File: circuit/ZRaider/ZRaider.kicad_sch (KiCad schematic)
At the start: 20 parts, among them J1 DE9_Socket, SW1 UP, SW2 DOWN, SW3 LEFT, SW4 RIGHT, SW5 Trigger, SW6 Calibrate

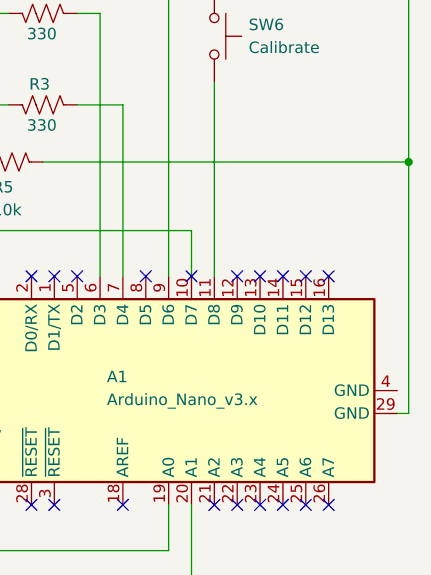
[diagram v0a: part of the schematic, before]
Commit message: adding last remaining connections
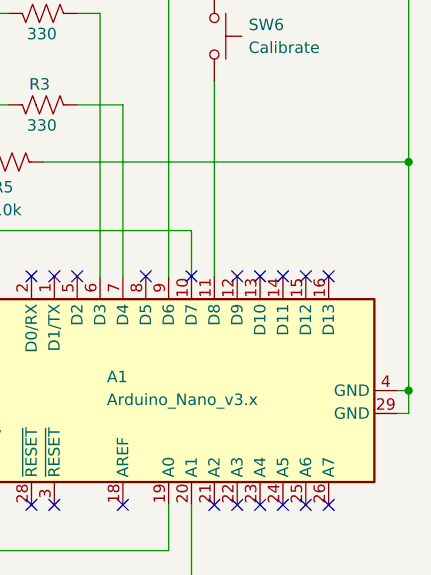
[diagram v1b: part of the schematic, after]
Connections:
- net at A1.29 (GND), C1.2, C2.2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: now also A1.4 (GND)
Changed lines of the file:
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@@
+	)
+	(junction
+		(at 236.22 119.38)
+		(diameter 0)
+		(color 0 0 0 0)
 	)
 	(junction
@@
 	(wire
 		(pts
+			(xy 236.22 119.38) (xy 236.22 121.92)
+		)
+		(stroke
+			(width 0)
+			(type default)
+		)
+	)
+	(wire
+		(pts
 			(xy 69.85 49.53) (xy 87.63 49.53)
 		)
@@
 	(wire
 		(pts
+			(xy 234.95 119.38) (xy 236.22 119.38)
+		)
+		(stroke
+			(width 0)
+			(type default)
+		)
+	)
+	(wire
+		(pts
 			(xy 212.09 146.05) (xy 212.09 132.08)
 		)
@@
 	(wire
 		(pts
-			(xy 236.22 93.98) (xy 236.22 121.92)
-		)
-		(stroke
+			(xy 236.22 93.98) (xy 236.22 119.38)
+		)
+		(stroke

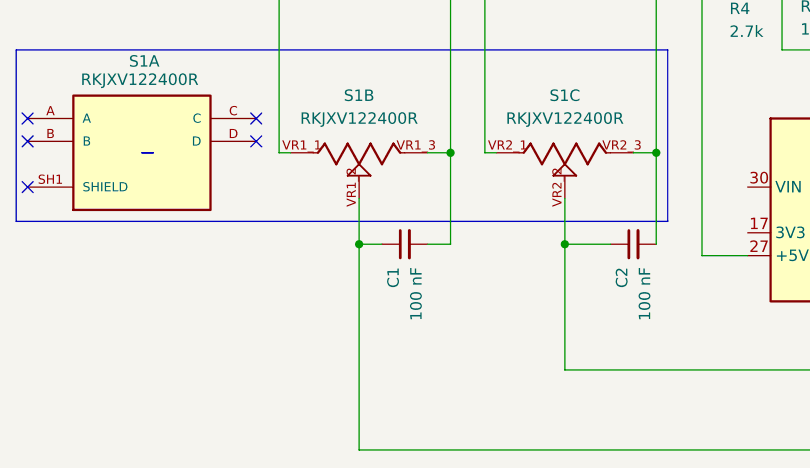
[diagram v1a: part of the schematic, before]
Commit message: updating layout to accomodate J1 size (actual) vs library
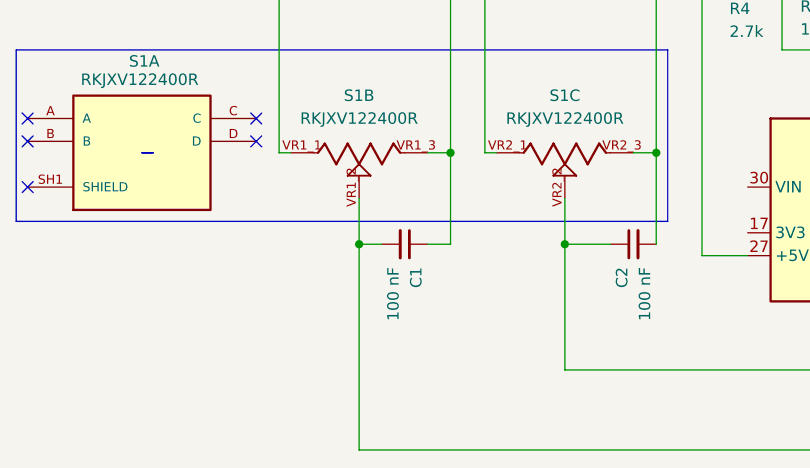
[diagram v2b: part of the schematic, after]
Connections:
- net at A1.29 (GND), A1.4 (GND), C2.2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: now also C1.1; no longer C1.2
- net at A1.20 (A1), S1.VR1_2: now also C1.2; no longer C1.1
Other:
- moved on the sheet: C1
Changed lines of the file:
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@@
 	(symbol
 		(lib_id "Device:C_Small")
-		(at 146.05 123.19 90)
-		(mirror x)
+		(at 146.05 123.19 270)
 		(unit 1)
 		(body_style 1)
@@
 		(in_pos_files yes)
 		(dnp no)
-		(fields_autoplaced yes)
 		(property "Reference" "C1"
-			(at 144.7862 125.73 0)
+			(at 147.3138 125.73 0)
 			(show_name no)
 			(do_not_autoplace no)
@@
 		)
 		(property "Value" "100 nF"
-			(at 147.3262 125.73 0)
+			(at 144.7738 125.73 0)
 			(show_name no)
 			(do_not_autoplace no)

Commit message: updating fuse footprint
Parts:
- F1: footprint Fuse:Fuse_0805_2012Metric_Pad1.15x1.40mm_HandSolder -> Fuse:Fuse_1812_4532Metric_Pad1.30x3.40mm_HandSolder
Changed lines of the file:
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@@
 			)
 		)
-		(property "Footprint" "Fuse:Fuse_0805_2012Metric_Pad1.15x1.40mm_HandSolder"
+		(property "Footprint" "Fuse:Fuse_1812_4532Metric_Pad1.30x3.40mm_HandSolder"
 			(at 180.34 77.47 0)
 			(hide yes)

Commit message: minor edits
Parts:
- removed D2: 1N4001, Diode_THT:D_DO-41_SOD81_P10.16mm_Horizontal, symbol Diode:1N4001
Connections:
- net at J1.5: now also R3.1
- no-connect marks 24 -> 25
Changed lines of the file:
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@@
+	)
+	(no_connect
+		(at 184.15 121.92)
 	)
 	(no_connect
@@
 	)
 	(no_connect
-		(at 212.09 106.68)
-	)
-	(no_connect
 		(at 194.31 106.68)
 	)
@@
 		(at 196.85 106.68)
 	)
+	(no_connect
+		(at 184.15 116.84)
+	)
 	(wire
 		(pts
@@
 	(wire
 		(pts
-			(xy 185.42 64.77) (xy 185.42 74.93)
-		)
-		(stroke
-			(width 0)
-			(type default)
-		)
-	)
-	(wire
-		(pts
 			(xy 87.63 91.44) (xy 102.87 91.44)
 		)
@@
 	(wire
 		(pts
-			(xy 185.42 82.55) (xy 185.42 87.63)
+			(xy 185.42 64.77) (xy 185.42 87.63)
 		)
 		(stroke
@@
 					(unit 1)
 				)
-			)
-		)
-	)
-	(symbol
-		(lib_id "Diode:1N4001")
-		(at 185.42 78.74 90)
-		(mirror x)
-		(unit 1)
-		(body_style 1)
-		(exclude_from_sim no)
-		(in_bom yes)
-		(on_board yes)
-		(in_pos_files yes)
-		(dnp no)
-		(property "Reference" "D2"
-			(at 182.88 78.74 0)
-			(show_name no)
-			(do_not_autoplace no)
-			(effects
-				(font
-					(size 1.27 1.27)
-				)
-			)
-		)
-		(property "Value" "1N4001"
-			(at 188.722 78.74 0)
-			(show_name no)
-			(do_not_autoplace no)
-			(effects
-				(font
-					(size 1.27 1.27)
-				)
-			)
-		)
-		(property "Footprint" "Diode_THT:D_DO-41_SOD81_P10.16mm_Horizontal"
-			(at 185.42 78.74 0)
-			(hide yes)
-			(show_name no)
-			(do_not_autoplace no)
-			(effects
-				(font
-					(size 1.27 1.27)
-				)
-			)
-		)
-		(property "Datasheet" "http://www.vishay.com/docs/88503/1n4001.pdf"
-			(at 185.42 78.74 0)
-			(hide yes)
-			(show_name no)
-			(do_not_autoplace no)
-			(effects
-				(font
-					(size 1.27 1.27)
-				)
-			)
-		)
-		(property "Description" "50V 1A General Purpose Rectifier Diode, DO-41"
-			(at 185.42 78.74 0)
-			(hide yes)
-			(show_name no)
-			(do_not_autoplace no)
-			(effects
-				(font
-					(size 1.27 1.27)
-				)
-			)
-		)
-		(property "Sim.Device" "D"
-			(at 185.42 78.74 0)
-			(hide yes)
-			(show_name no)
-			(do_not_autoplace no)
-			(effects
-				(font
-					(size 1.27 1.27)
-				)
-			)
-		)
-		(property "Sim.Pins" "1=K 2=A"
-			(at 185.42 78.74 0)
-			(hide yes)
-			(show_name no)
-			(do_not_autoplace no)
-			(effects
-				(font
-					(size 1.27 1.27)
-				)
-			)
-		)
-		(pin "1"
-		)
-		(pin "2"
-		)
-		(instances
-			(project "ZRaider"
-				(path "/cee3fad8-cd38-4e35-ae79-7b381e15c120"
-					(reference "D2")
-					(unit 1)
-				)

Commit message: re-add D2
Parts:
- added D2: 1N4001, Diode_THT:D_DO-41_SOD81_P10.16mm_Horizontal, symbol Diode:1N4001
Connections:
- net at J1.5: now also D2.1 (K); no longer R3.1
- new net: D2.2 (A), R3.1
- no-connect marks 25 -> 26
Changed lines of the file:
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@@
+	)
+	(no_connect
+		(at 129.54 109.22)
+	)
+	(no_connect
+		(at 212.09 106.68)
+	)
+	(no_connect
+		(at 194.31 106.68)
+	)
+	(no_connect
+		(at 219.71 106.68)
+	)
+	(no_connect
+		(at 204.47 132.08)
+	)
+	(no_connect
+		(at 104.14 116.84)
+	)
+	(no_connect
+		(at 199.39 106.68)
+	)
+	(no_connect
+		(at 217.17 132.08)
+	)
+	(no_connect
+		(at 194.31 132.08)
+	)
+	(no_connect
+		(at 129.54 111.76)
+	)
+	(no_connect
+		(at 224.79 132.08)
 	)
 	(no_connect
@@
 	)
 	(no_connect
-		(at 129.54 109.22)
-	)
-	(no_connect
-		(at 194.31 106.68)
-	)
-	(no_connect
-		(at 219.71 106.68)
-	)
-	(no_connect
-		(at 204.47 132.08)
-	)
-	(no_connect
-		(at 104.14 116.84)
-	)
-	(no_connect
-		(at 199.39 106.68)
-	)
-	(no_connect
-		(at 217.17 132.08)
-	)
-	(no_connect
-		(at 194.31 132.08)
-	)
-	(no_connect
-		(at 129.54 111.76)
-	)
-	(no_connect
-		(at 224.79 132.08)
-	)
-	(no_connect
 		(at 196.85 132.08)
 	)
@@
 	(wire
 		(pts
+			(xy 185.42 64.77) (xy 185.42 74.93)
+		)
+		(stroke
+			(width 0)
+			(type default)
+		)
+	)
+	(wire
+		(pts
 			(xy 87.63 91.44) (xy 102.87 91.44)
 		)
@@
 	(wire
 		(pts
-			(xy 185.42 64.77) (xy 185.42 87.63)
+			(xy 185.42 82.55) (xy 185.42 87.63)
 		)
 		(stroke
@@
 					(unit 1)
 				)
+			)
+		)
+	)
+	(symbol
+		(lib_id "Diode:1N4001")
+		(at 185.42 78.74 90)
+		(mirror x)
+		(unit 1)
+		(body_style 1)
+		(exclude_from_sim no)
+		(in_bom yes)
+		(on_board yes)
+		(in_pos_files yes)
+		(dnp no)
+		(property "Reference" "D2"
+			(at 182.88 78.74 0)
+			(show_name no)
+			(do_not_autoplace no)
+			(effects
+				(font
+					(size 1.27 1.27)
+				)
+			)
+		)
+		(property "Value" "1N4001"
+			(at 188.722 78.74 0)
+			(show_name no)
+			(do_not_autoplace no)
+			(effects
+				(font
+					(size 1.27 1.27)
+				)
+			)
+		)
+		(property "Footprint" "Diode_THT:D_DO-41_SOD81_P10.16mm_Horizontal"
+			(at 185.42 78.74 0)
+			(hide yes)
+			(show_name no)
+			(do_not_autoplace no)
+			(effects
+				(font
+					(size 1.27 1.27)
+				)
+			)
+		)
+		(property "Datasheet" "http://www.vishay.com/docs/88503/1n4001.pdf"
+			(at 185.42 78.74 0)
+			(hide yes)
+			(show_name no)
+			(do_not_autoplace no)
+			(effects
+				(font
+					(size 1.27 1.27)
+				)
+			)
+		)
+		(property "Description" "50V 1A General Purpose Rectifier Diode, DO-41"
+			(at 185.42 78.74 0)
+			(hide yes)
+			(show_name no)
+			(do_not_autoplace no)
+			(effects
+				(font
+					(size 1.27 1.27)
+				)
+			)
+		)
+		(property "Sim.Device" "D"
+			(at 185.42 78.74 0)
+			(hide yes)
+			(show_name no)
+			(do_not_autoplace no)
+			(effects
+				(font
+					(size 1.27 1.27)
+				)
+			)
+		)
+		(property "Sim.Pins" "1=K 2=A"
+			(at 185.42 78.74 0)
+			(hide yes)
+			(show_name no)
+			(do_not_autoplace no)
+			(effects
+				(font
+					(size 1.27 1.27)
+				)
+			)
+		)
+		(pin "1"
+		)
+		(pin "2"
+		)
+		(instances
+			(project "ZRaider"
+				(path "/cee3fad8-cd38-4e35-ae79-7b381e15c120"
+					(reference "D2")
+					(unit 1)
+				)
